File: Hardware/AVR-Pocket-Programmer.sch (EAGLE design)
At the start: 37 parts, among them Q1 12 MHz, U1 ATTINY2313-20S, U2 74ACT125D, X2 USBSMD

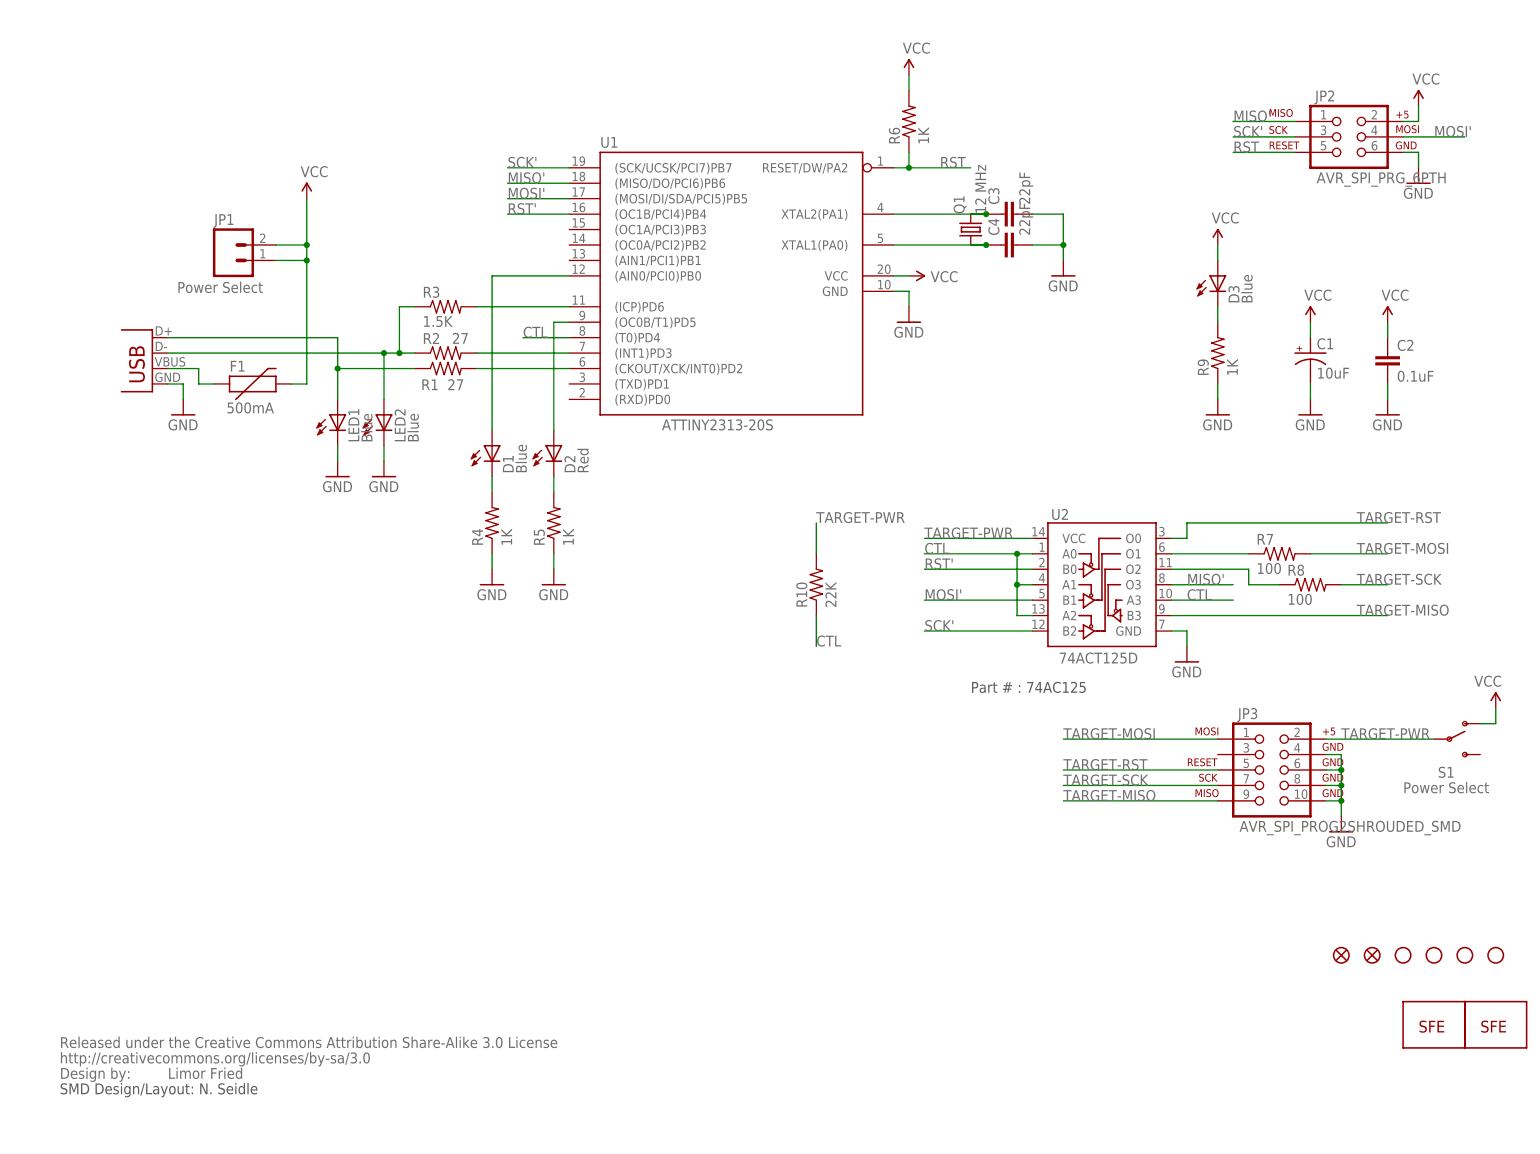
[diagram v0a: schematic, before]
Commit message: QC Revision - second round
In addition to the three previous changes:

1.) Updated PTC footprint
2.) General schematic cleanup
3.) OSHW and Creative Commons info
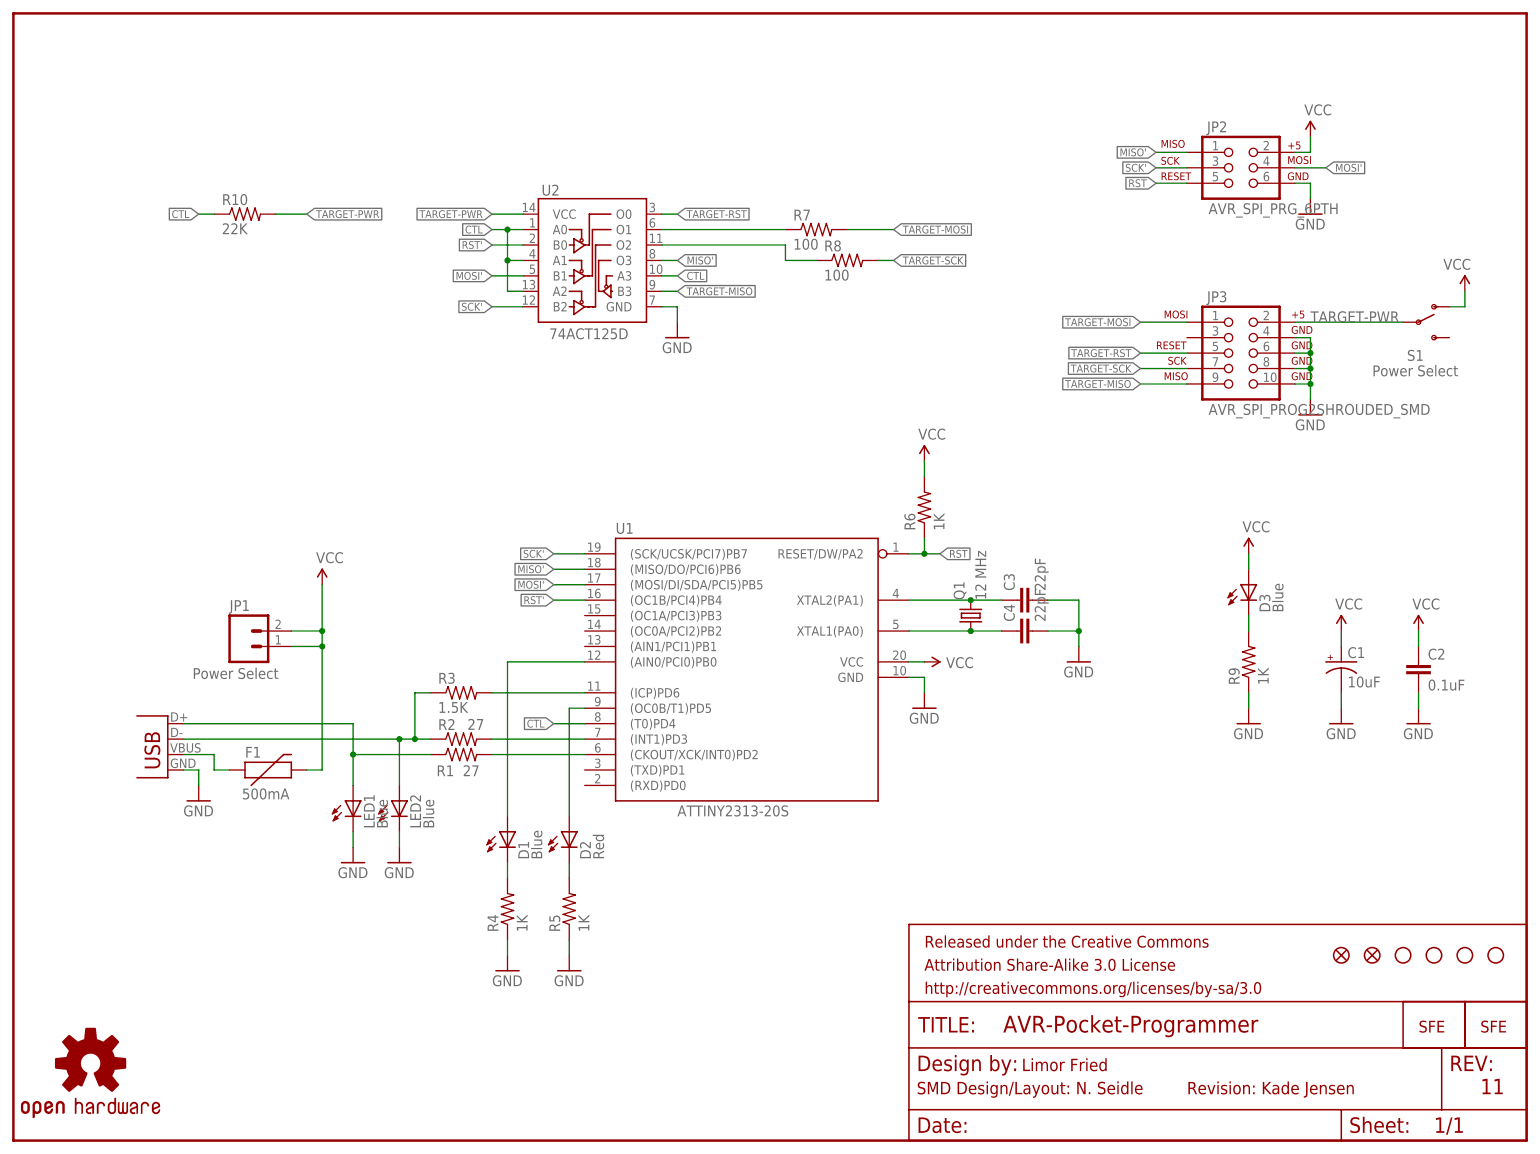
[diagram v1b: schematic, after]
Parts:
- removed U$9: CREATIVE_COMMONS, SparkFun:CREATIVE_COMMONS
- added FRAME1: FRAME-LETTER, SparkFun-Aesthetics:FRAME-LETTER
- added LOGO1: OSHW-LOGOM, SparkFun-Aesthetics:OSHW-LOGOM
- F1: device SparkFun:PTCSMD -> SparkFun-PowerIC:PTCSMD-W
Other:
- note added: "11"
- note added: "Revision: Kade Jensen"
- note removed: "Part # : 74AC125"
- moved on the sheet: C1, C2, C3, C4, D1, D2, D3, F1, JP1, JP2, JP3, LED1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
